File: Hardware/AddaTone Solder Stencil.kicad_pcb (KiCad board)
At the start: 2 copper layers, 60 x 110 mm, 78 parts, among them U1 STM32F446RETx, U2 ICE40UP5K-SG48ITR, U3 MCP6004, U4 PCM5100APW, U5 TL072, U6 LD1117S12TR, U7 LM1117-3.3, Y1 ECS-12MHz

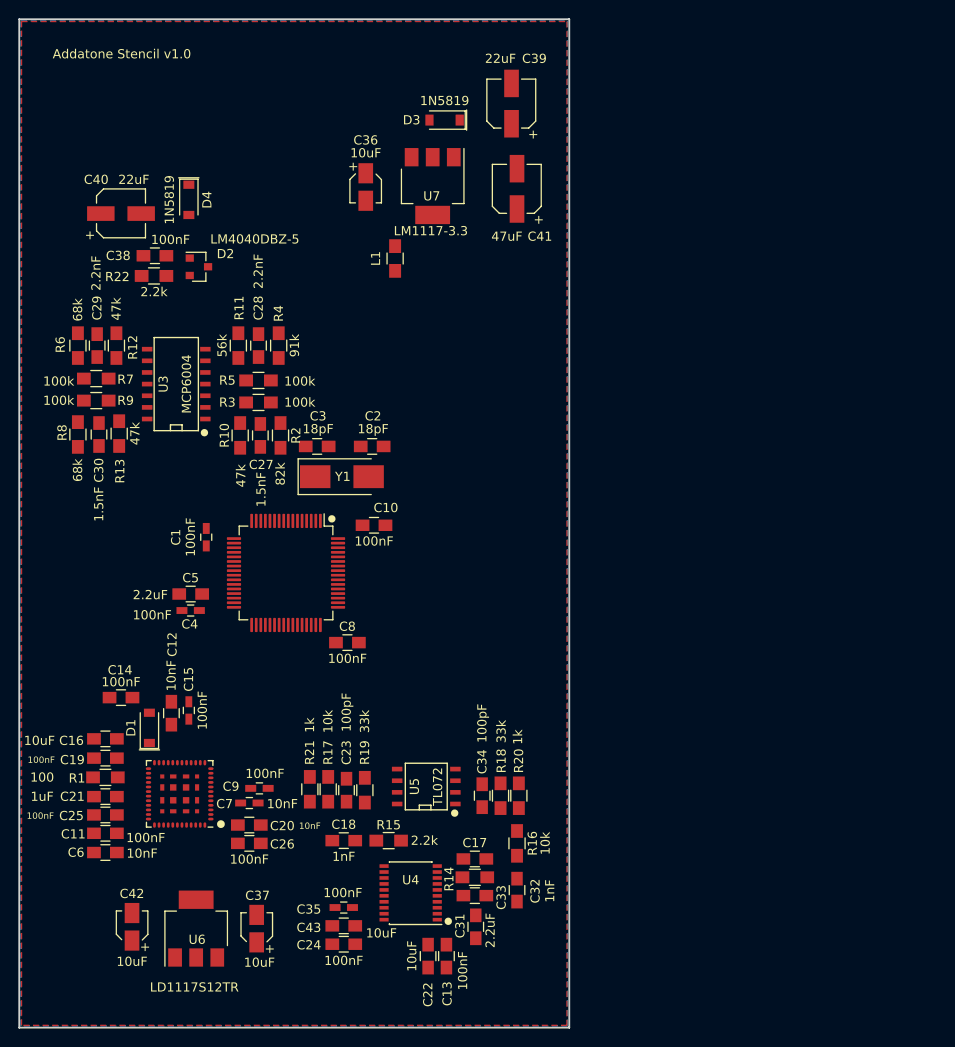
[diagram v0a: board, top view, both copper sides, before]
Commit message: Fixes to schematic (missing resistor on 1.2V LDO); Created new implementation to support production board; added FPGA tester project
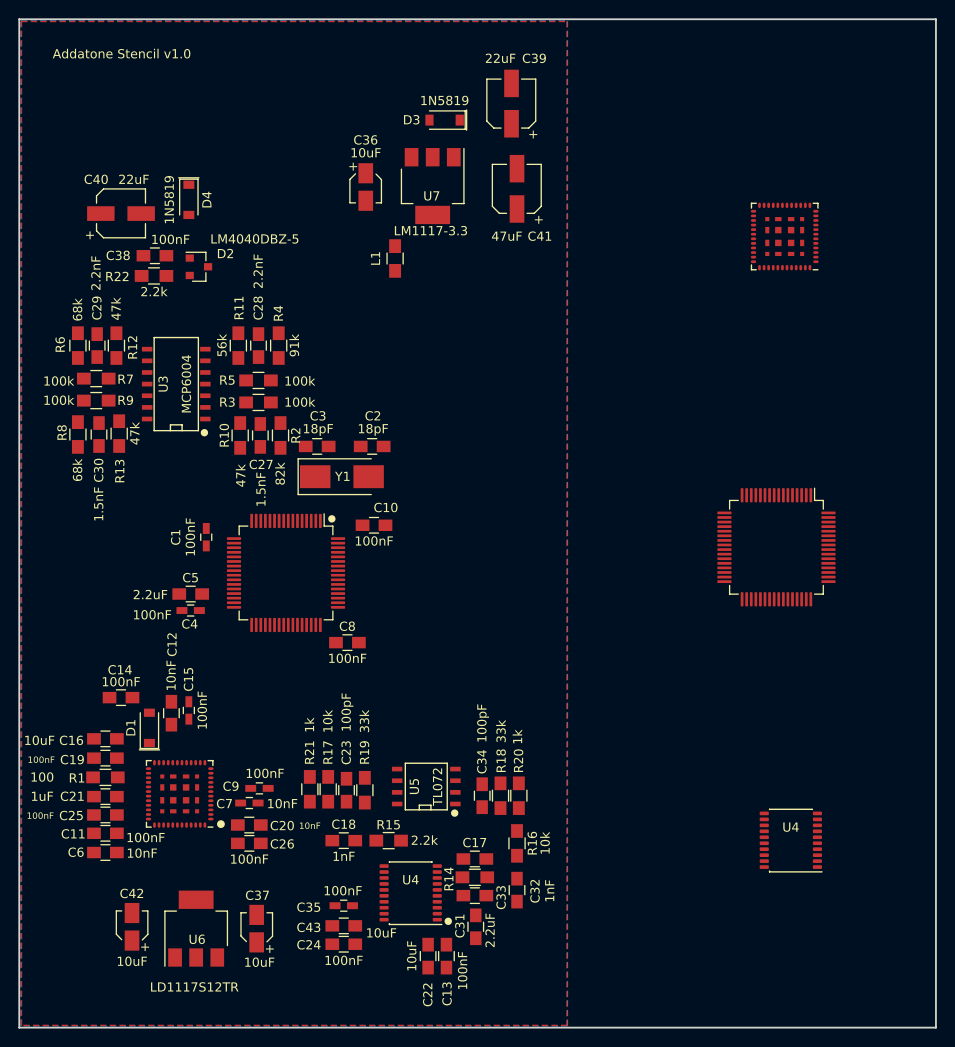
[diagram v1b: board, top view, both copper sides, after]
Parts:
- added U1: STM32F446RETx, Package_QFP:LQFP-64_10x10mm_P0.5mm, F.Cu at (182.6, 107.6)
- added U2: ICE40UP5K-SG48ITR, Custom_Footprints:ICE40_QFN-48-stencil, F.Cu at (183.5, 73.7)
- added U4: PCM5100APW, Custom_Footprints:SSOP-20_4.4x6.5mm_Pitch0.65mm_Round_Pads, F.Cu at (184.2, 139.6)
- U4: footprint Housings_SSOP:SSOP-20_4.4x6.5mm_Pitch0.65mm -> Custom_Footprints:SSOP-20_4.4x6.5mm_Pitch0.65mm_Round_Pads
- moved C35 0.20 mm to (135.4, 146.7)
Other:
- board size 60 x 110 mm -> 100 x 110 mm
